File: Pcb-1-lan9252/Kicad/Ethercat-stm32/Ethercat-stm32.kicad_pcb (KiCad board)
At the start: 2 copper layers, 94.5 x 59.2 mm, 134 parts, among them J1 Conn_01x02_Pin, J10 Conn_01x06_Pin, J11 Conn_01x06_Pin, J12 Conn_01x06_Pin, J13 Stepper 1, J14 Stepper 2, J2 Serial usart1, J3 STLINK, J4 I2C bus2, J5 DAC1, J6 Encoder 1, J7 Encoder 2, J8 Encoder 3, J9 Encoder 4, SW1 SW_Push, U1 LAN9252_PT, U2 AT24CS32-SSHM, U3 AMS1117-3.3, U4 STM32F407VGT6, Y1 25MHz, Y2 8 MHz

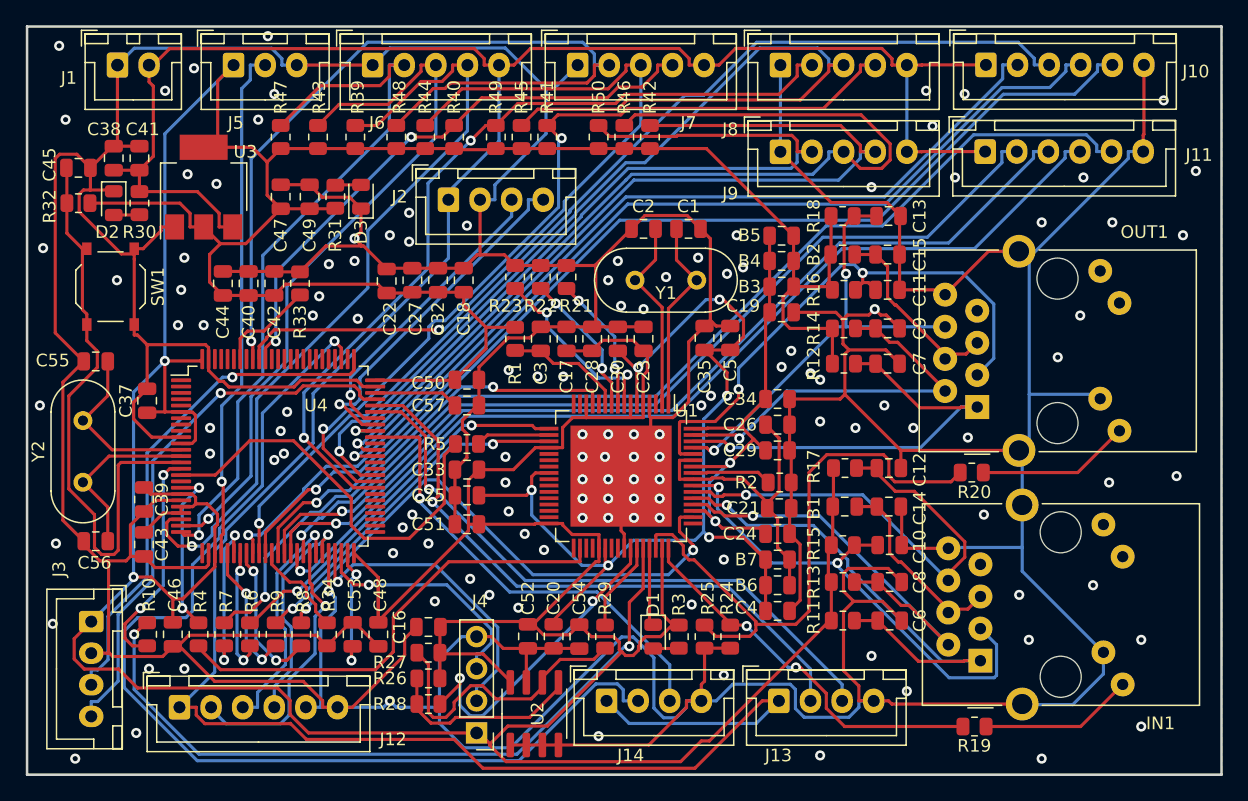
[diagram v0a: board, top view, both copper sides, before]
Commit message: Fixed 4-layer files
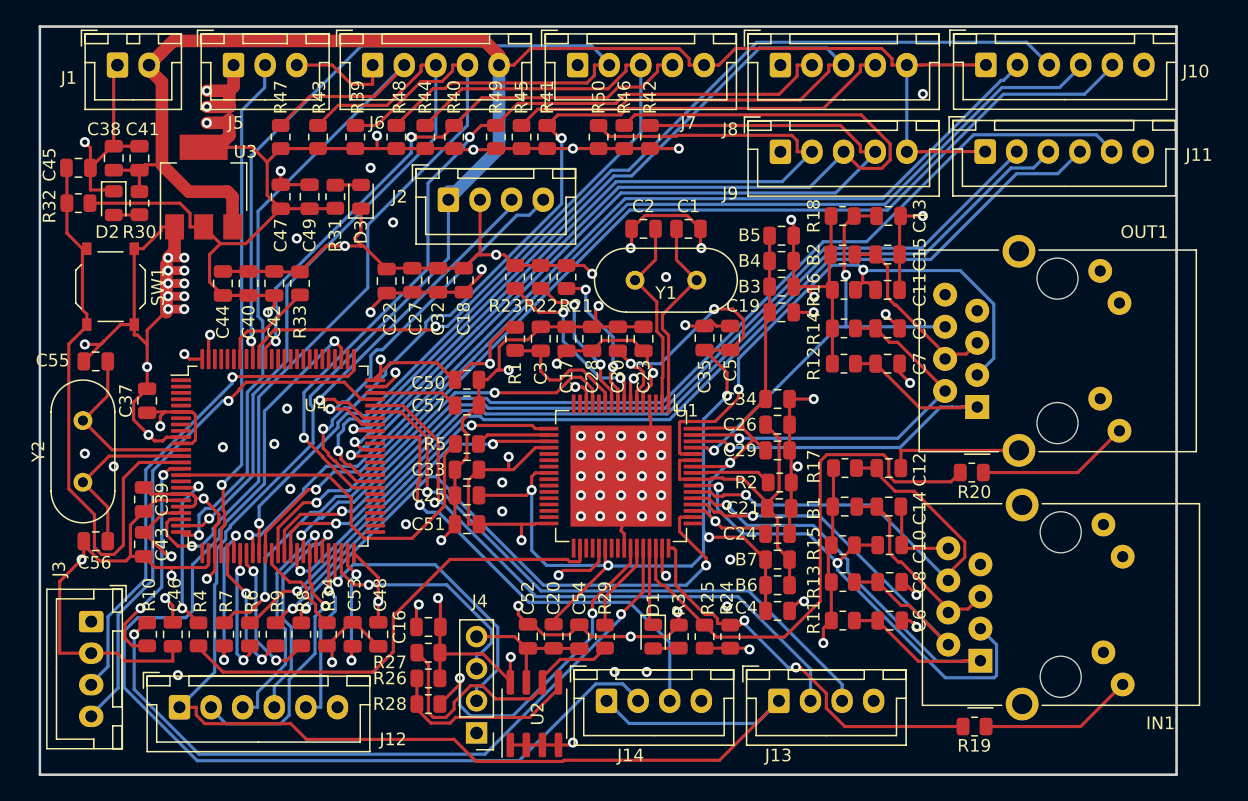
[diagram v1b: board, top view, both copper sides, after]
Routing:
- net +3.3V: track 451.2 -> 564.9 mm, vias 2 -> 35
- net GND: track 665.1 -> 751.1 mm, vias 125 -> 85
- net GPIO1: track 47.6 -> 42.8 mm
- net Net-(U1-D5/AD5/OUTVALID/SCS#): track 44.5 -> 47.7 mm
- net +1V2: track 80.0 -> 83.1 mm
- net RX: track 23.9 -> 26.6 mm
- net SYNC1: track 32.6 -> 30.5 mm
- net NRST: track 47.2 -> 45.3 mm
- net Net-(U1-IRQ): track 58.8 -> 57.0 mm
- net GPIO0: track 30.5 -> 32.1 mm
- net Net-(U1-~{RST}): track 9.52 -> 10.9 mm
- net I2C_SDA: track 25.1 -> 26.5 mm
- net STEP2_STEP: track 36.6 -> 37.9 mm
- net FXLOSA: track 10.8 -> 11.8 mm
- net TX: track 27.7 -> 28.7 mm
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- added copper zone on In2.Cu, net +3.3V
- added copper zone on In1.Cu, net GND
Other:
- board size 94.5 x 59.2 mm -> 89.9 x 59.2 mm
- copper layers 2 -> 4
